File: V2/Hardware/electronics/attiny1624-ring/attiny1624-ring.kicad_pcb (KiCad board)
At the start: 2 copper layers, 50 x 50 mm, 23 parts, among them J1 CHAIN_RING, J3 STEPPER_DRIVER_IN, J4 HOME_SENSOR, J5 UPDI_2X3, U1 ATtiny1624-SS

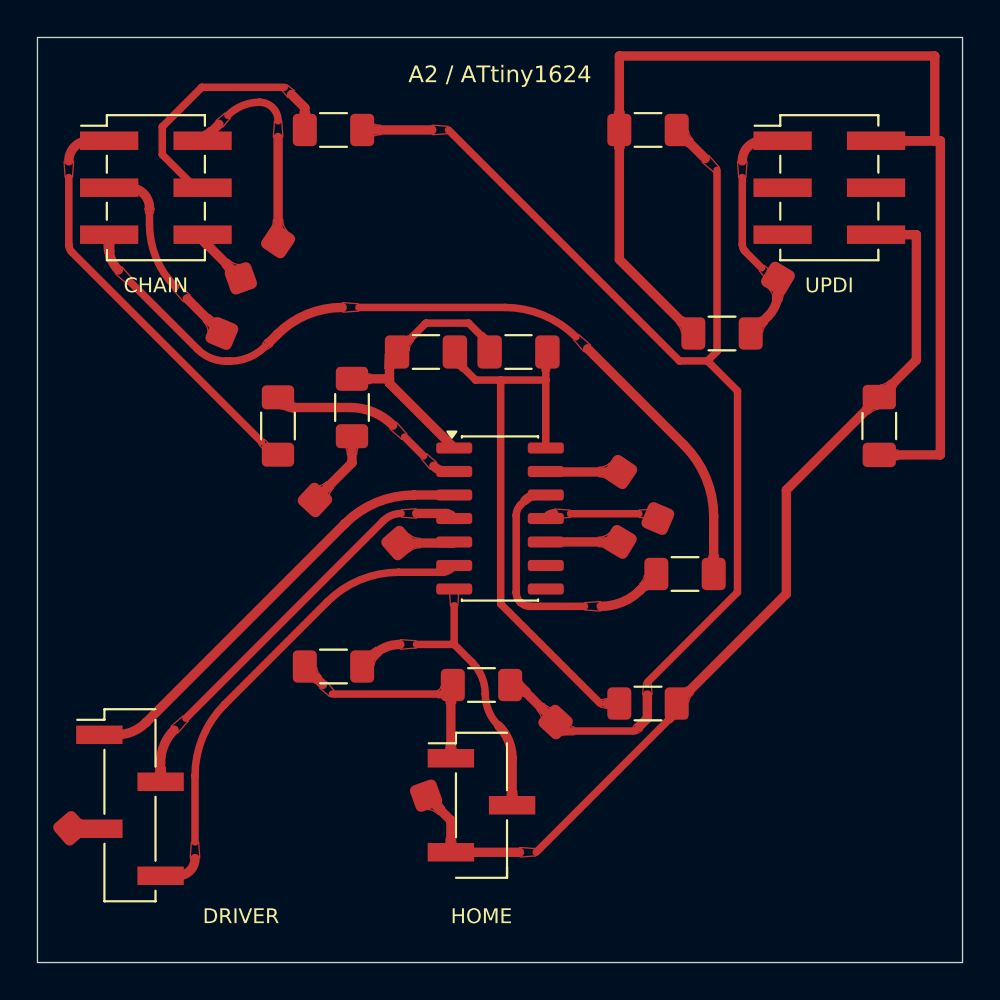
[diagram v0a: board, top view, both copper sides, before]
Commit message: Align ATtiny1624 board with module firmware
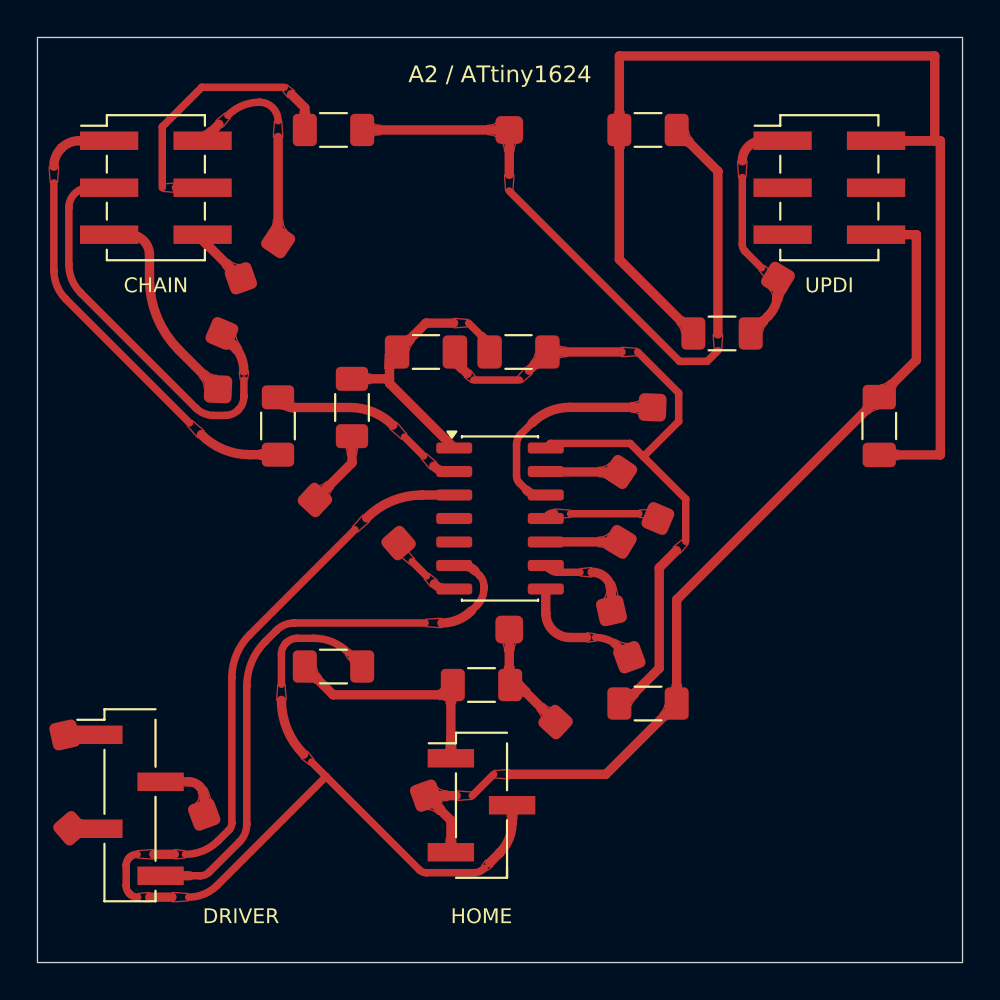
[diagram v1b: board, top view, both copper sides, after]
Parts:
- added JP14: INSULATED MOTOR1 LINK 30.3mm, Alphabets:WireLink_30.3mm_SMD, F.Cu at (115.2, 134.3)
- added JP15: INSULATED MOTOR2 LINK 24.5mm, Alphabets:WireLink_24.5mm_SMD, F.Cu at (119.5, 137.8)
- added JP16: INSULATED MAIN POWER LINK 27.0mm, Alphabets:WireLink_27.0mm_SMD, F.Cu at (124.5, 118.5)
- JP8: value 0R DATA output bridge 1206 -> INSULATED DATA_OUT LINK 23.5mm; footprint Resistor_SMD:R_1206_3216Metric_Pad1.30x1.75mm_HandSolder -> Alphabets:WireLink_23.5mm_SMD
- U1: value ATtiny1624-SS -> ATtiny1624-SSU
- moved JP8 16.5 mm to (120.5, 119.5), turned to 177.6 degrees
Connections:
- J3 pad 1: MOTOR1 -> MOTOR1_DRIVER
- J3 pad 2: MOTOR2 -> MOTOR2_DRIVER
- JP1 pad 2: +5V_MAIN -> +5V_MAIN_TOP
- JP2 pad 2: +5V_MAIN -> +5V_MAIN_TOP
- U1 pad 3: MOTOR1 -> HOME
- U1 pad 4: MOTOR2 -> unconnected-(U1-PA6-Pad4)
- U1 pad 5: MOTOR3_U1 -> unconnected-(U1-PA7-Pad5)
- U1 pad 7: HOME -> MOTOR3_U1
- U1 pad 8: unconnected-(U1-PB1-Pad8) -> MOTOR2_U1
- U1 pad 9: unconnected-(U1-PB0-Pad9) -> MOTOR1_U1
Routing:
- net +5V_MAIN: track 65.4 -> 6.30 mm
- net HOME: track 16.2 -> 67.2 mm
- net +5V_MAIN_TOP: track 0.00 -> 37.6 mm
- net DATA_OUT_CHAIN: track 42.5 -> 11.3 mm
- net MOTOR1: track 24.2 -> 0.00 mm
- net MOTOR2: track 21.2 -> 0.00 mm
- net DATA_CHAIN_IN: track 9.72 -> 22.5 mm
- net MOTOR2_U1: track 0.00 -> 6.39 mm
- net GND_U1: track 31.4 -> 37.5 mm
- net MOTOR4: track 25.4 -> 30.7 mm
- net MOTOR1_U1: track 0.00 -> 4.61 mm
- net MOTOR2_DRIVER: track 0.00 -> 3.75 mm
- net LATCH_CONN: track 21.6 -> 24.1 mm
- net DATA_OUT_U1: track 14.0 -> 12.0 mm
- net MOTOR1_DRIVER: track 0.00 -> 1.87 mm
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- added copper zone on F.Cu, net +5V_MAIN_TOP
- added copper zone on F.Cu, net MOTOR1_DRIVER
- added copper zone on F.Cu, net MOTOR1_U1
- added copper zone on F.Cu, net MOTOR2_DRIVER
- added copper zone on F.Cu, net MOTOR2_U1
- removed copper zone on F.Cu, net MOTOR1
- removed copper zone on F.Cu, net MOTOR2
